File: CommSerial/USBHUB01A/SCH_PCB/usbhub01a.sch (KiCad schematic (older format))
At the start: 51 parts, among them J1 OverCurrent, J12 I2C, J2 Test & Misc Signals, M1 HOLE, M2 HOLE, M3 HOLE, M4 HOLE, U1 CAT24C04YI-GT3OSCT-ND, U2 TUSB8041IPAPRQ1, Y1 24MHz

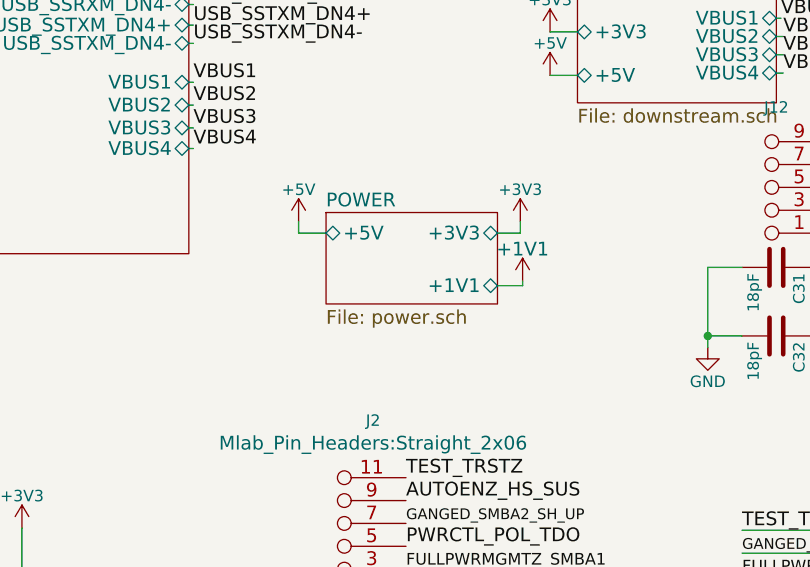
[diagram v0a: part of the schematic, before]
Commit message: Vyhozený vypínač, přidaný "Distribution Load Switch"
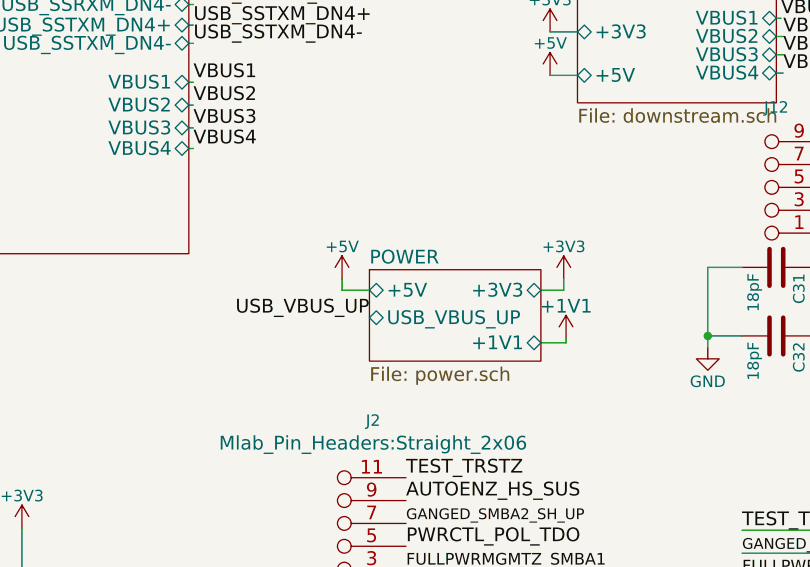
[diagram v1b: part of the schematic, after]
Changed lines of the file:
@@
 $EndDescr
 $Sheet
-S 4210 2710 750  400
+S 4400 2960 750  400
 U 55551F88
 F0 "POWER" 60
 F1 "power.sch" 60
-F2 "+5V" B L 4210 2800 60
-F3 "+3V3" B R 4960 2800 60
-F4 "+1V1" B R 4960 3030 60
+F2 "+5V" B L 4400 3050 60
+F3 "+3V3" B R 5150 3050 60
+F4 "+1V1" B R 5150 3280 60
+F5 "USB_VBUS_UP" B L 4400 3170 60
 $EndSheet
 $Sheet
@@
 L +3V3 #PWR030
 U 1 1 55EC3BF3
-P 5060 2750
-F 0 "#PWR030" H 5060 2600 50  0001 C CNN
-F 1 "+3V3" H 5060 2890 50  0000 C CNN
-F 2 "" H 5060 2750 60  0000 C CNN
-F 3 "" H 5060 2750 60  0000 C CNN
-	1    5060 2750
+P 5250 3000
+F 0 "#PWR030" H 5250 2850 50  0001 C CNN
+F 1 "+3V3" H 5250 3140 50  0000 C CNN
+F 2 "" H 5250 3000 60  0000 C CNN
+F 3 "" H 5250 3000 60  0000 C CNN
+	1    5250 3000
 	1    0    0    -1
 $EndComp
@@
 L +1V1 #PWR031
 U 1 1 55EC598E
-P 5070 3010
-F 0 "#PWR031" H 5070 2860 60  0001 C CNN
-F 1 "+1V1" H 5070 3150 60  0000 C CNN
-F 2 "" H 5070 3010 60  0000 C CNN
-F 3 "" H 5070 3010 60  0000 C CNN
-	1    5070 3010
+P 5260 3260
+F 0 "#PWR031" H 5260 3110 60  0001 C CNN
+F 1 "+1V1" H 5260 3400 60  0000 C CNN
+F 2 "" H 5260 3260 60  0000 C CNN
+F 3 "" H 5260 3260 60  0000 C CNN
+	1    5260 3260
 	1    0    0    -1
 $EndComp
@@
 L +5V #PWR032
 U 1 1 55EC99D0
-P 4090 2750
-F 0 "#PWR032" H 4090 2600 50  0001 C CNN
-F 1 "+5V" H 4090 2890 50  0000 C CNN
-F 2 "" H 4090 2750 60  0000 C CNN
-F 3 "" H 4090 2750 60  0000 C CNN
-	1    4090 2750
+P 4280 3000
+F 0 "#PWR032" H 4280 2850 50  0001 C CNN
+F 1 "+5V" H 4280 3140 50  0000 C CNN
+F 2 "" H 4280 3000 60  0000 C CNN
+F 3 "" H 4280 3000 60  0000 C CNN
+	1    4280 3000
 	1    0    0    -1
 $EndComp
@@
 	3610 790  3630 790
 Wire Wire Line
-	4960 3030 5070 3030
-Wire Wire Line
-	5070 3030 5070 3010
-Wire Wire Line
-	4960 2800 5060 2800
-Wire Wire Line
-	5060 2800 5060 2750
-Wire Wire Line
-	4210 2800 4090 2800
-Wire Wire Line
-	4090 2800 4090 2750
+	5150 3280 5260 3280
+Wire Wire Line
+	5260 3280 5260 3260
+Wire Wire Line
+	5150 3050 5250 3050
+Wire Wire Line
+	5250 3050 5250 3000
+Wire Wire Line
+	4400 3050 4280 3050
+Wire Wire Line
+	4280 3050 4280 3000
 Wire Wire Line
 	5190 2110 5310 2110
@@
 Text Label 4560 3870 0    60   ~ 0
 TEST_TRSTZ
+Text Label 4400 3170 2    60   ~ 0
+USB_VBUS_UP
 $EndSCHEMATC

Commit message: USB-Hub-funkcni finalni verze
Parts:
- R17: value 10k -> 10k 1%
- R18: value 90k9 -> 90k9 1%
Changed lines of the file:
@@
 P 8830 850
 F 0 "R17" V 8910 850 50  0000 C CNN
-F 1 "10k" V 8830 850 50  0000 C CNN
+F 1 "10k 1%" V 8750 850 50  0000 C CNN
 F 2 "Mlab_R:SMD-0603" V 8760 850 30  0001 C CNN
 F 3 "" H 8830 850 30  0000 C CNN
@@
 P 9230 700
 F 0 "R18" V 9310 700 50  0000 C CNN
-F 1 "90k9" V 9230 700 50  0000 C CNN
+F 1 "90k9 1%" V 9130 670 50  0000 C CNN
 F 2 "Mlab_R:SMD-0603" V 9160 700 30  0001 C CNN
 F 3 "" H 9230 700 30  0000 C CNN
